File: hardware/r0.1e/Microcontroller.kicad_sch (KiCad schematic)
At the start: 100 parts, among them J10 UART, J2 USB_C, J3 OLED, J8 +12V, J9 STLink, SW1 Button Up, SW2 Button Down, SW3 Reset, SW4 Button Escape, SW5 Button Left, SW6 Button Enter, SW7 Button Right, U10 STM32F405RGTx, U11 TPS73233, U2 TP6841S6, U3 USBLC6-2, U4 W25Q16, X1 12 MHz TCXO, Y1 8 MHz, Y2 32 kHz

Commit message: WIP r0.1e power switch
👀
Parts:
- removed BT1: Coin, Battery:BatteryHolder_Keystone_3000_1x12mm, symbol Device:Battery_Cell
- removed C28, C68: 100n, pkl_dipol:C_0603, symbol pkl_device:pkl_C_Small
- removed C66, C67: 12p, pkl_dipol:C_0603, symbol pkl_device:pkl_C_Small
- removed R21: 10k, pkl_dipol:R_0603, symbol pkl_device:pkl_R_Small
- removed R22: 22, pkl_dipol:R_0603, symbol pkl_device:pkl_R_Small
- removed R47, R48: 4k7, pkl_dipol:R_0603, symbol pkl_device:pkl_R_Small
- removed RV1: 50k, M17-SmartMic:PTR901, symbol M17-SmartMic:R_Potentiometer_Switch
- removed U4: W25Q16, Package_SO:SOIC-8_3.9x4.9mm_P1.27mm, symbol pkl_memory:W25Q
- removed Y2: 32 kHz, Crystal:Crystal_SMD_MicroCrystal_CC8V-T1A-2Pin_2.0x1.2mm, symbol Device:Crystal_Small
- added D7: BAT54C, Package_TO_SOT_SMD:SOT-23, symbol Diode:BAT54C
- added Q4: IRLML6402, Package_TO_SOT_SMD:SOT-23, symbol Transistor_FET:IRLML6402
- added Q5: MMBT3904, Package_TO_SOT_SMD:SOT-23, symbol Transistor_BJT:MMBT3904
- added R63: 100k, symbol Device:R_Small
- added R64, R66, R67: 10k, symbol Device:R_Small
- added R65: 220k, symbol Device:R_Small
- added SW8: Button Power, pkl_buttons_switches:SW_SPST_PTS645, symbol Switch:SW_Push
- C22, C24, C26, X1: now not fitted
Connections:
- net GND: now also Q5.2 (E), R65.2
- net VIN: now also Q4.2 (S), R66.1, SW8.1
- net at FB2.2: now also Q4.3 (D)
- net GPIO_POWER: now reaches U10.50 (PA15)
- net GPIO_POWER: now also D7.1
- new net: D7.3, R64.1
- new net: Q5.1 (B), R64.2
- new net: Q4.1 (G), R66.2, R67.1
- new net: Q5.3 (C), R67.2
- new net: D7.2, R63.2, R65.1
- new net: R63.1, SW8.2
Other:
- note removed: "DNP"
- note removed: "SPI Flash currently not installed."
- moved on the sheet: C1, C11, C13, C14, C16, C17, C18, C19, C23, C25, C27, C4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

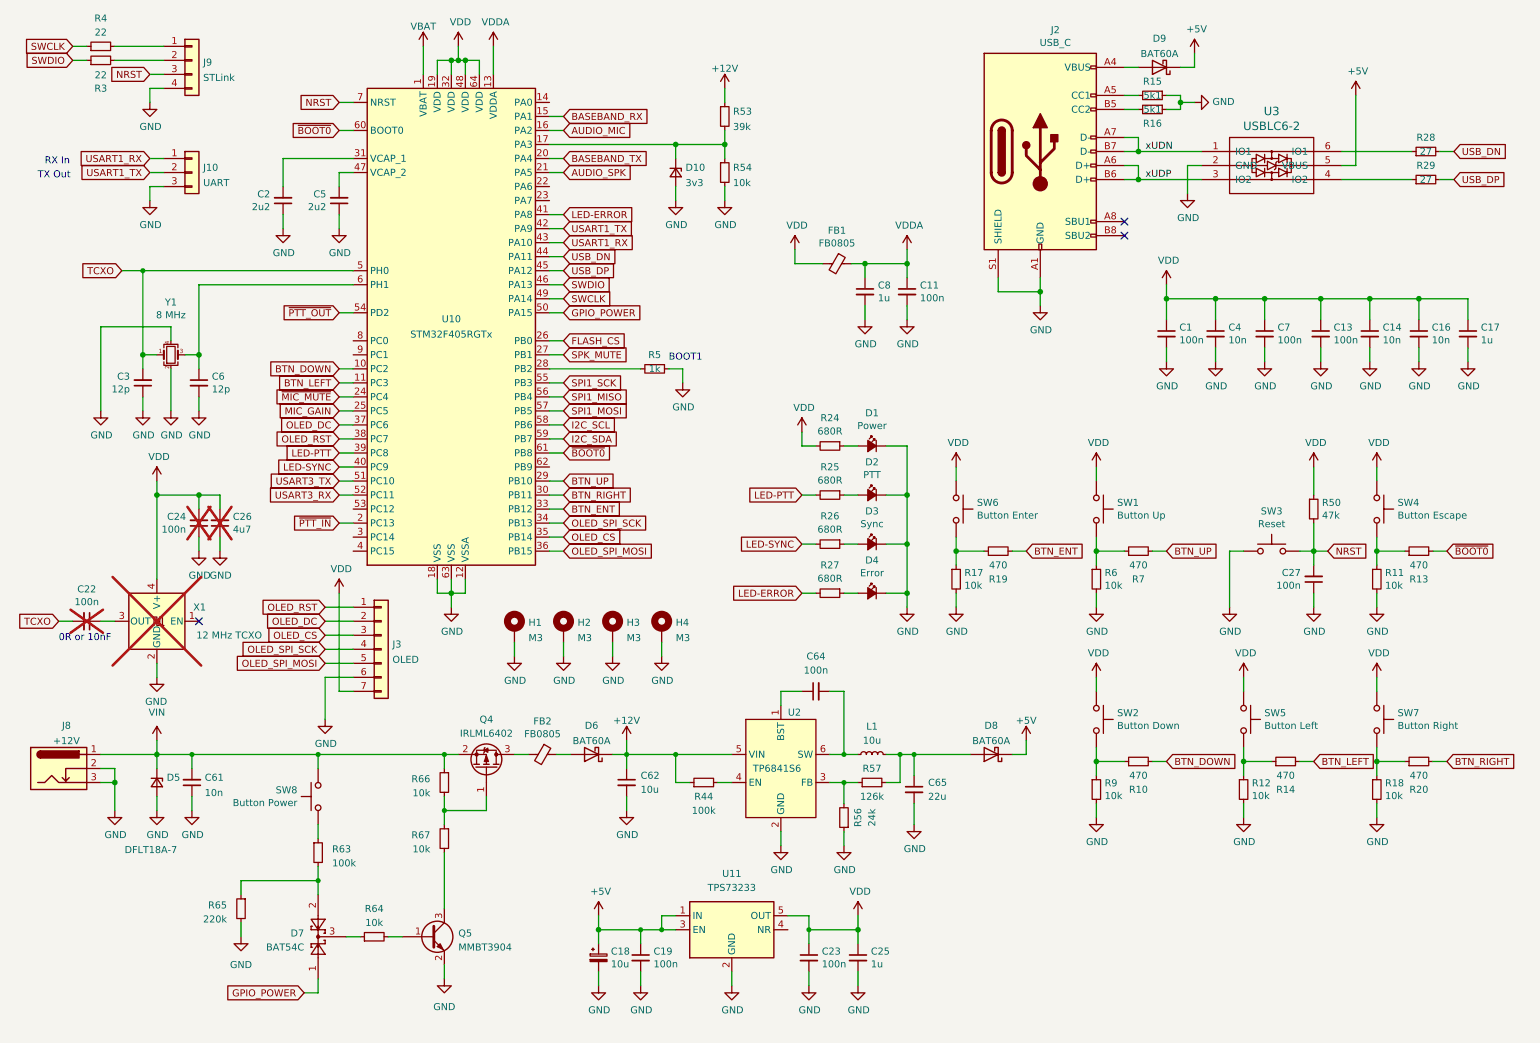
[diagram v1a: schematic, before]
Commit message: Updates to the latching power switch
WIP r0.1e, schematics can be considered final
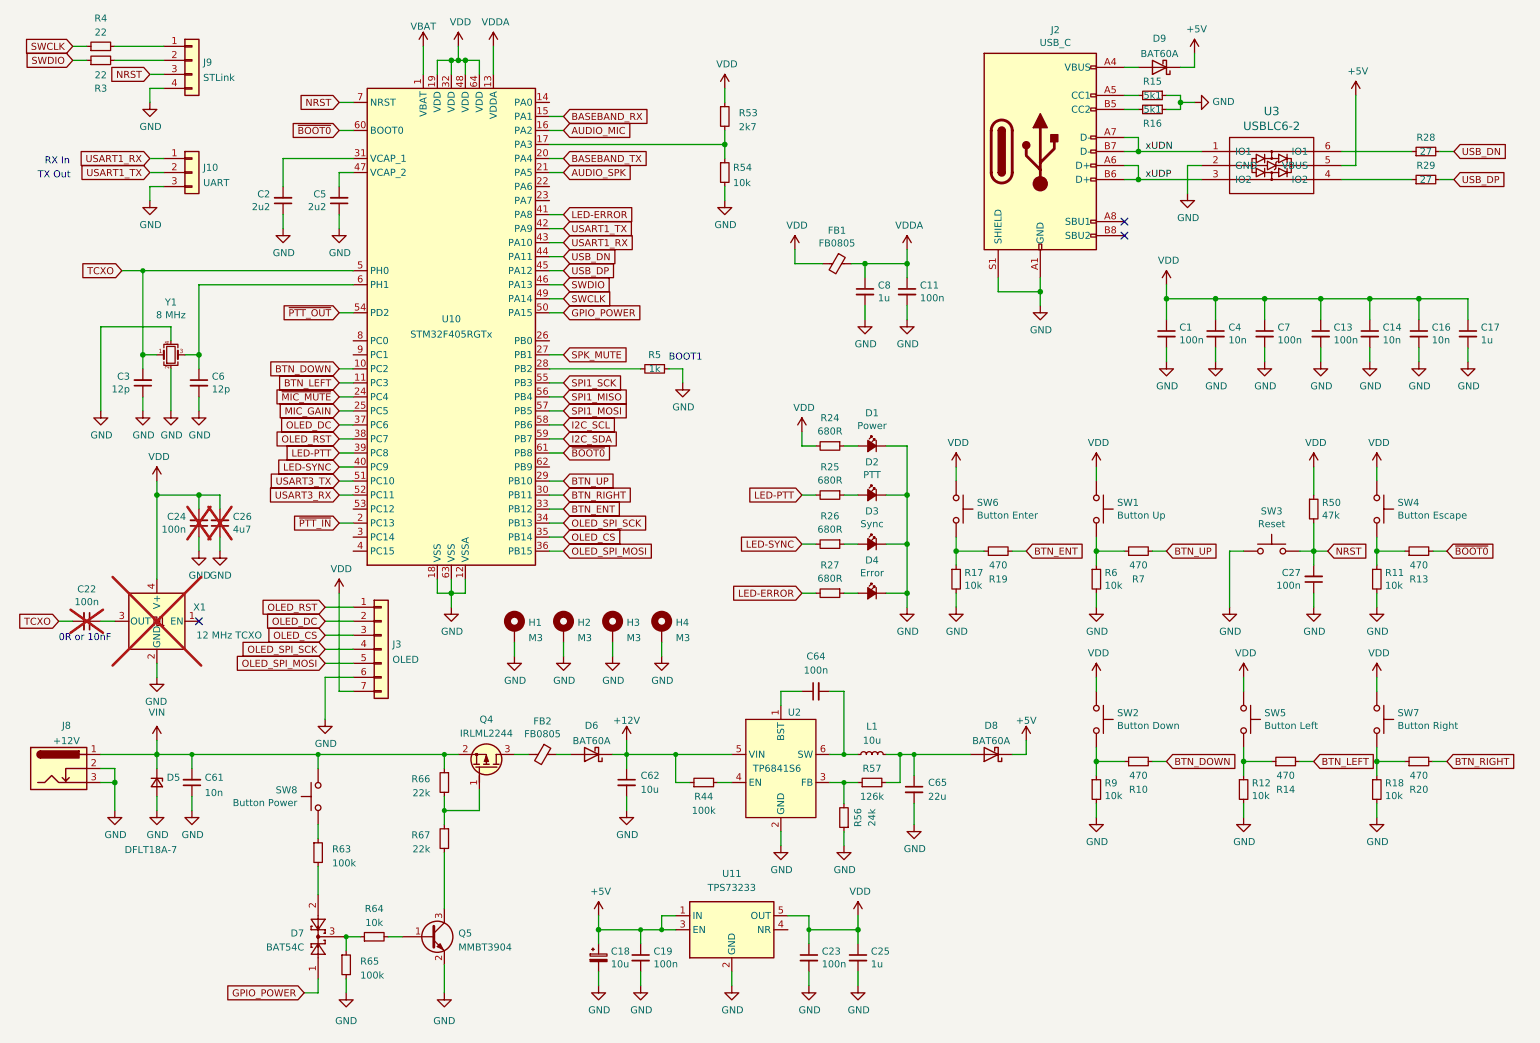
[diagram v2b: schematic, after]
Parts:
- removed D10: 3v3, Diode_SMD:D_SOD-523, symbol Device:D_Zener_Small
- removed Q4: IRLML6402, Package_TO_SOT_SMD:SOT-23, symbol Transistor_FET:IRLML6402
- added Q4: IRLML2244, Package_TO_SOT_SMD:SOT-23, symbol PCM_Transistor_MOSFET_AKL:IRLML2244
- R53: value 39k -> 2k7
- R63, R64: footprint (none) -> pkl_dipol:R_0603
- R65: value 220k -> 100k; footprint (none) -> pkl_dipol:R_0603
- R66, R67: value 10k -> 22k; footprint (none) -> pkl_dipol:R_0603
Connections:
- net +12V: no longer R53.1
- net VDD: now also R53.1
- net VIN: now also Q4.2 (S)
- net at D7.3, R64.1: now also R65.1
- net at R66.2, R67.1: now also Q4.1 (G)
- net at FB2.2: now also Q4.3 (D)
- net at D7.2, R63.2: no longer R65.1
- net FLASH_CS: no longer names the net of U10.26 (PB0)
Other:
- moved on the sheet: R65

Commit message: Gold Master r0.1e
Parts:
- removed D6: BAT60A, Diode_SMD:D_SOD-323, symbol Diode:BAT60A
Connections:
- net +12V: now also FB2.1
- net at D7.3, R64.1: no longer R65.1
- net at Q5.1 (B), R64.2: now also R65.1
- no-connect marks 3 -> 12
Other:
- moved on the sheet: R65
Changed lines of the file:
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@@
   (junction (at 173.99 58.42) (diameter 1.016) (color 0 0 0 0)
   )
-  (junction (at 72.39 180.34) (diameter 0) (color 0 0 0 0)
-  )
   (junction (at 30.48 152.4) (diameter 1.016) (color 0 0 0 0)
   )
@@
   (junction (at 38.1 100.33) (diameter 1.016) (color 0 0 0 0)
   )
+  (junction (at 81.28 180.34) (diameter 0) (color 0 0 0 0)
+  )
   (junction (at 215.9 43.18) (diameter 1.016) (color 0 0 0 0)
   )
@@
   (junction (at 165.1 179.07) (diameter 1.016) (color 0 0 0 0)
   )
+  (no_connect (at 109.22 95.25))
   (no_connect (at 213.36 50.8))
   (no_connect (at 213.36 53.34))
+  (no_connect (at 109.22 44.45))
   (no_connect (at 45.72 123.19))
+  (no_connect (at 73.66 110.49))
+  (no_connect (at 109.22 46.99))
+  (no_connect (at 109.22 72.39))
+  (no_connect (at 73.66 72.39))
+  (no_connect (at 73.66 107.95))
+  (no_connect (at 73.66 74.93))
+  (no_connect (at 73.66 102.87))
   (wire (pts (xy 91.44 115.57) (xy 91.44 118.11))
     (stroke (width 0) (type solid))
@@
     (stroke (width 0) (type solid))
   )
+  (wire (pts (xy 81.28 180.34) (xy 82.55 180.34))
+    (stroke (width 0) (type default))
+  )
   (wire (pts (xy 270.51 38.1) (xy 273.05 38.1))
     (stroke (width 0) (type solid))
@@
     (stroke (width 0) (type solid))
   )
-  (wire (pts (xy 72.39 187.96) (xy 72.39 190.5))
+  (wire (pts (xy 81.28 187.96) (xy 81.28 190.5))
     (stroke (width 0) (type default))
   )
@@
     (stroke (width 0) (type solid))
   )
-  (wire (pts (xy 110.49 147.32) (xy 113.03 147.32))
+  (wire (pts (xy 110.49 147.32) (xy 123.19 147.32))
     (stroke (width 0) (type solid))
   )
@@
     (stroke (width 0) (type solid))
   )
-  (wire (pts (xy 120.65 147.32) (xy 123.19 147.32))
-    (stroke (width 0) (type solid))
-  )
-  (wire (pts (xy 72.39 182.88) (xy 72.39 180.34))
+  (wire (pts (xy 81.28 182.88) (xy 81.28 180.34))
     (stroke (width 0) (type default))
   )
@@
     (stroke (width 0) (type default))
   )
-  (wire (pts (xy 80.01 180.34) (xy 82.55 180.34))
+  (wire (pts (xy 80.01 180.34) (xy 81.28 180.34))
     (stroke (width 0) (type default))
   )
@@
     )
   )
-  (symbol (lib_name "GND_1") (lib_id "power:GND") (at 72.39 190.5 0) (mirror y) (unit 1)
+  (symbol (lib_name "GND_1") (lib_id "power:GND") (at 81.28 190.5 0) (mirror y) (unit 1)
     (in_bom yes) (on_board yes) (dnp no) (fields_autoplaced)
-    (property "Reference" "#PWR086" (at 72.39 196.85 0)
+    (property "Reference" "#PWR086" (at 81.28 196.85 0)
       (effects (font (size 1.27 1.27)) hide)
     )
-    (property "Value" "GND" (at 72.39 195.58 0)
+    (property "Value" "GND" (at 81.28 195.58 0)
       (effects (font (size 1.27 1.27)))
     )
-    (property "Footprint" "" (at 72.39 190.5 0)
+    (property "Footprint" "" (at 81.28 190.5 0)
       (effects (font (size 1.27 1.27)) hide)
     )
-    (property "Datasheet" "" (at 72.39 190.5 0)
+    (property "Datasheet" "" (at 81.28 190.5 0)
       (effects (font (size 1.27 1.27)) hide)
     )
@@
     )
   )
-  (symbol (lib_id "Device:R_Small") (at 72.39 185.42 0) (unit 1)
+  (symbol (lib_id "Device:R_Small") (at 81.28 185.42 0) (unit 1)
     (in_bom yes) (on_board yes) (dnp no)
-    (property "Reference" "R65" (at 74.93 184.785 0)
+    (property "Reference" "R65" (at 83.82 184.785 0)
       (effects (font (size 1.27 1.27)) (justify left))
     )
-    (property "Value" "100k" (at 74.93 187.325 0)
+    (property "Value" "100k" (at 83.82 187.325 0)
       (effects (font (size 1.27 1.27)) (justify left))
     )
-    (property "Footprint" "pkl_dipol:R_0603" (at 72.39 185.42 0)
+    (property "Footprint" "pkl_dipol:R_0603" (at 81.28 185.42 0)
       (effects (font (size 1.27 1.27)) hide)
     )
-    (property "Datasheet" "~" (at 72.39 185.42 0)
+    (property "Datasheet" "~" (at 81.28 185.42 0)
       (effects (font (size 1.27 1.27)) hide)
     )
@@
         )
       )
-    )
-  )
-  (symbol (lib_id "Diode:BAT60A") (at 116.84 147.32 180) (unit 1)
-    (in_bom yes) (on_board yes) (dnp no) (fields_autoplaced)
-    (property "Reference" "D6" (at 116.84 142.0834 0)
-      (effects (font (size 1.27 1.27)))
-    )
-    (property "Value" "BAT60A" (at 116.84 144.8585 0)
-      (effects (font (size 1.27 1.27)))
-    )
-    (property "Footprint" "Diode_SMD:D_SOD-323" (at 116.84 142.875 0)
-      (effects (font (size 1.27 1.27)) hide)
-    )
-    (property "Datasheet" "https://www.infineon.com/dgdl/Infineon-BAT60ASERIES-DS-v01_01-en.pdf?fileId=db3a304313d846880113def70c9304a9" (at 116.84 147.32 0)
-      (effects (font (size 1.27 1.27)) hide)
-    )
-    (pin "1")
-    (pin "2")
-    (instances
-      (project "M17-SmartMic"
-        (path "/59592280-3207-432b-a891-cd517ec5cf12/00000000-0000-0000-0000-0000612c95ef"
-          (reference "D6") (unit 1)
-        )
-      )

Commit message: Sorted some MPNs
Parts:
- D5: MPN (none) -> DFLT18A-7
- D8: MPN (none) -> BAT60AE6327HTSA1
- J8: MPN (none) -> FC681465ST
- L1: MPN (none) -> IHLP2525CZER100M01; Partno IHLP2525CZER100M01 -> (none)
- Q4: MPN (none) -> IRLML2244TRPbF
- Q5: MPN (none) -> MMBT3904
- U10: MPN (none) -> STM32F405RGTx
- U3: MPN (none) -> USBLC6-2-SC6
